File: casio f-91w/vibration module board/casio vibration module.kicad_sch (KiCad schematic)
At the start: 7 parts, among them M1 Motor_DC, Q1 IRLML2803TRPBF

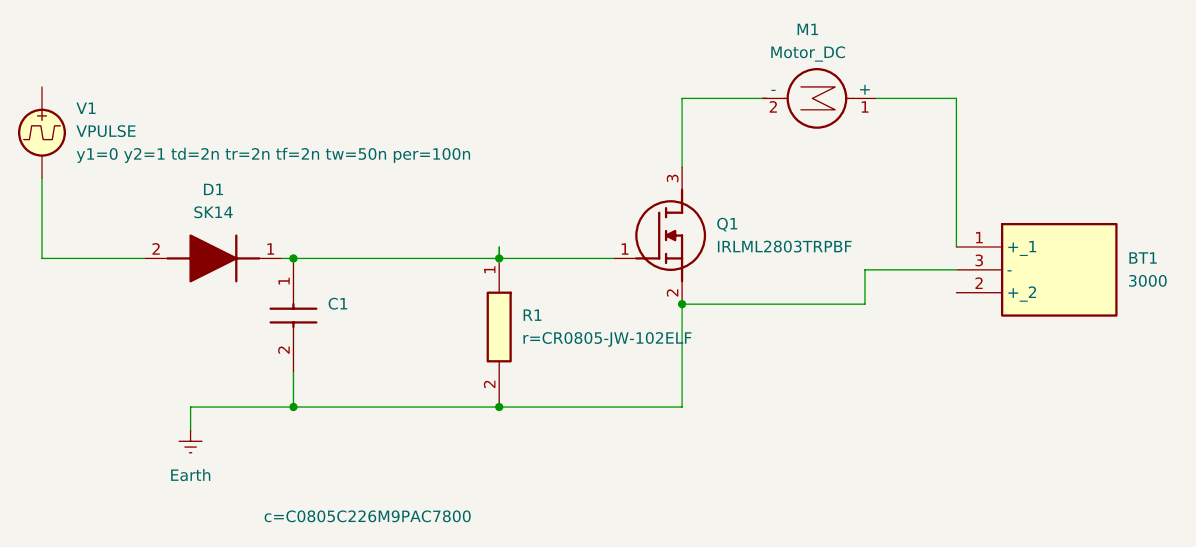
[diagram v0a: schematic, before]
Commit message: Update vibration module to use 100k resistor
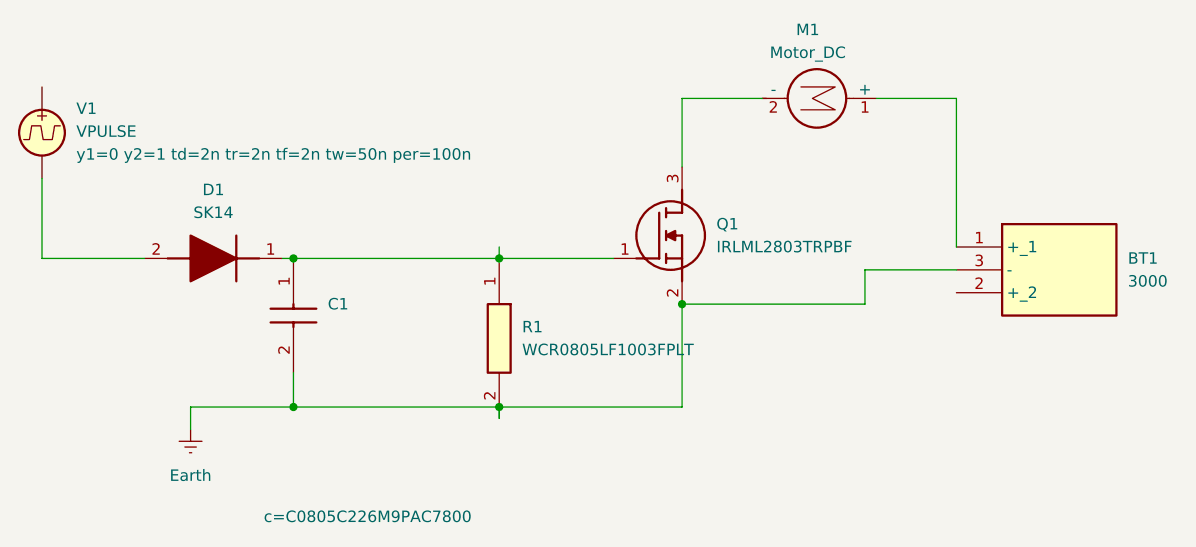
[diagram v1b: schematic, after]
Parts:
- removed R1: ${SIM.PARAMS}, RESC2012X60N, symbol CR0805-JW-102ELF:CR0805-JW-102ELF
- added R1: WCR0805LF1003FPLT, RESC2013X65N, symbol WCR0805LF1003FPLT:WCR0805LF1003FPLT
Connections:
- net Earth: now also R1.2
- net at C1.1, D1.1 (K), Q1.1 (G): now also R1.1
